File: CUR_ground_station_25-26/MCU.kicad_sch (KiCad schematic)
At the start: 14 parts, among them J4 Conn_01x04_Pin, SW7 PTS815SJM250SMTRLFS, SW8 PTS815SJM250SMTRLFS, U1 ESP32-S3-WROOM-1

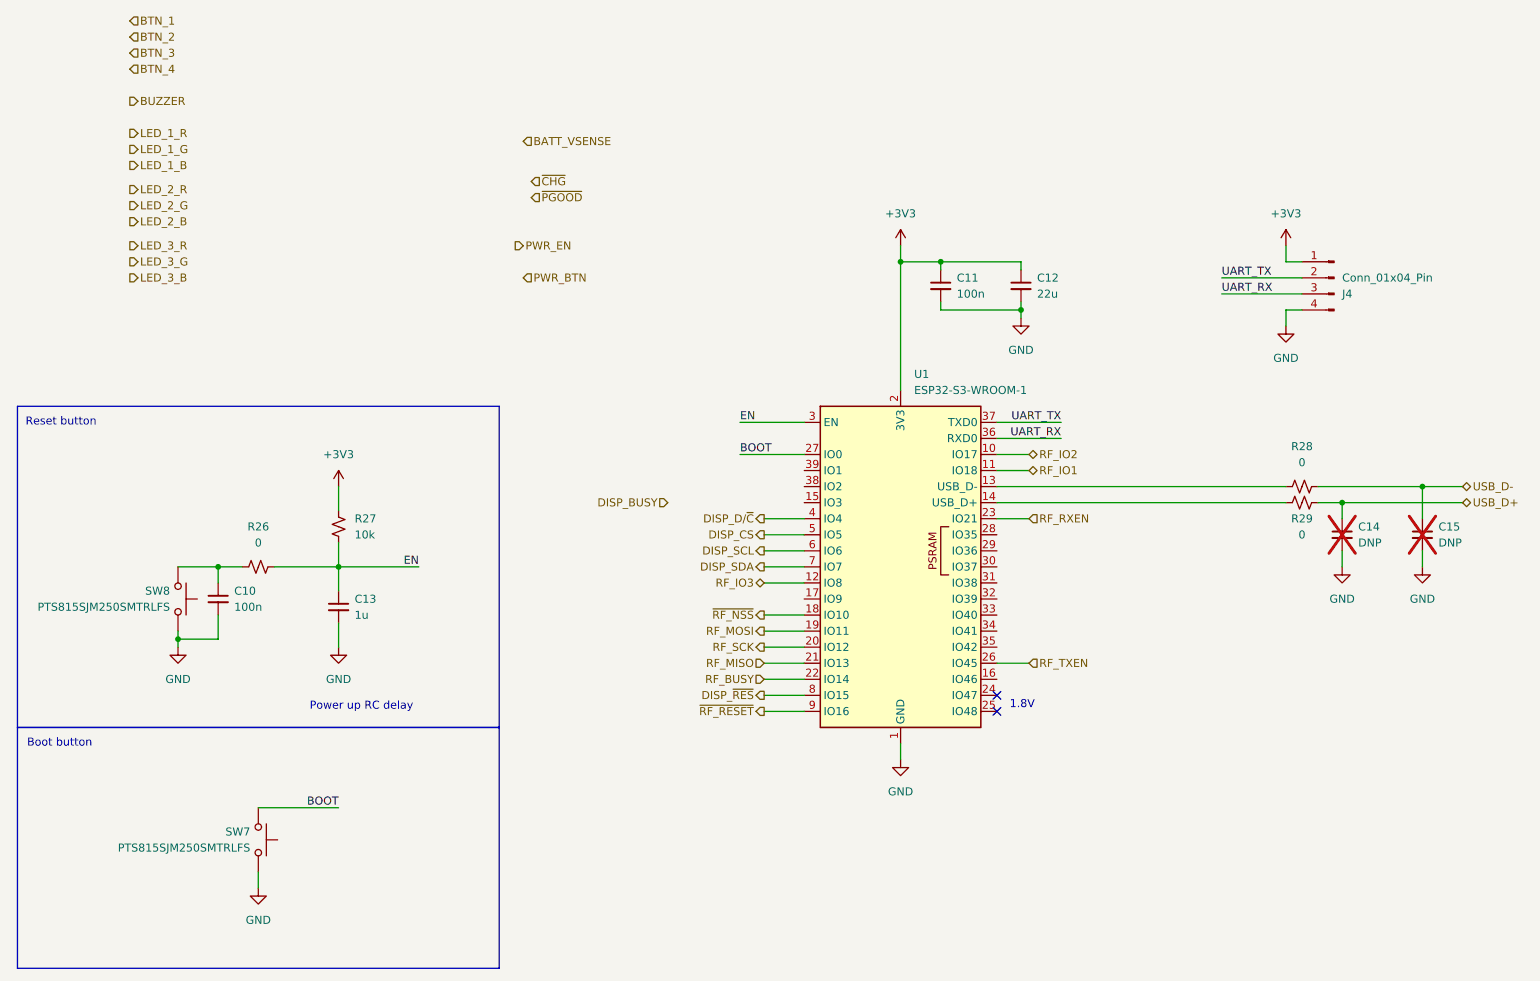
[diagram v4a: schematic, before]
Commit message: Change MCU, hookup more pins
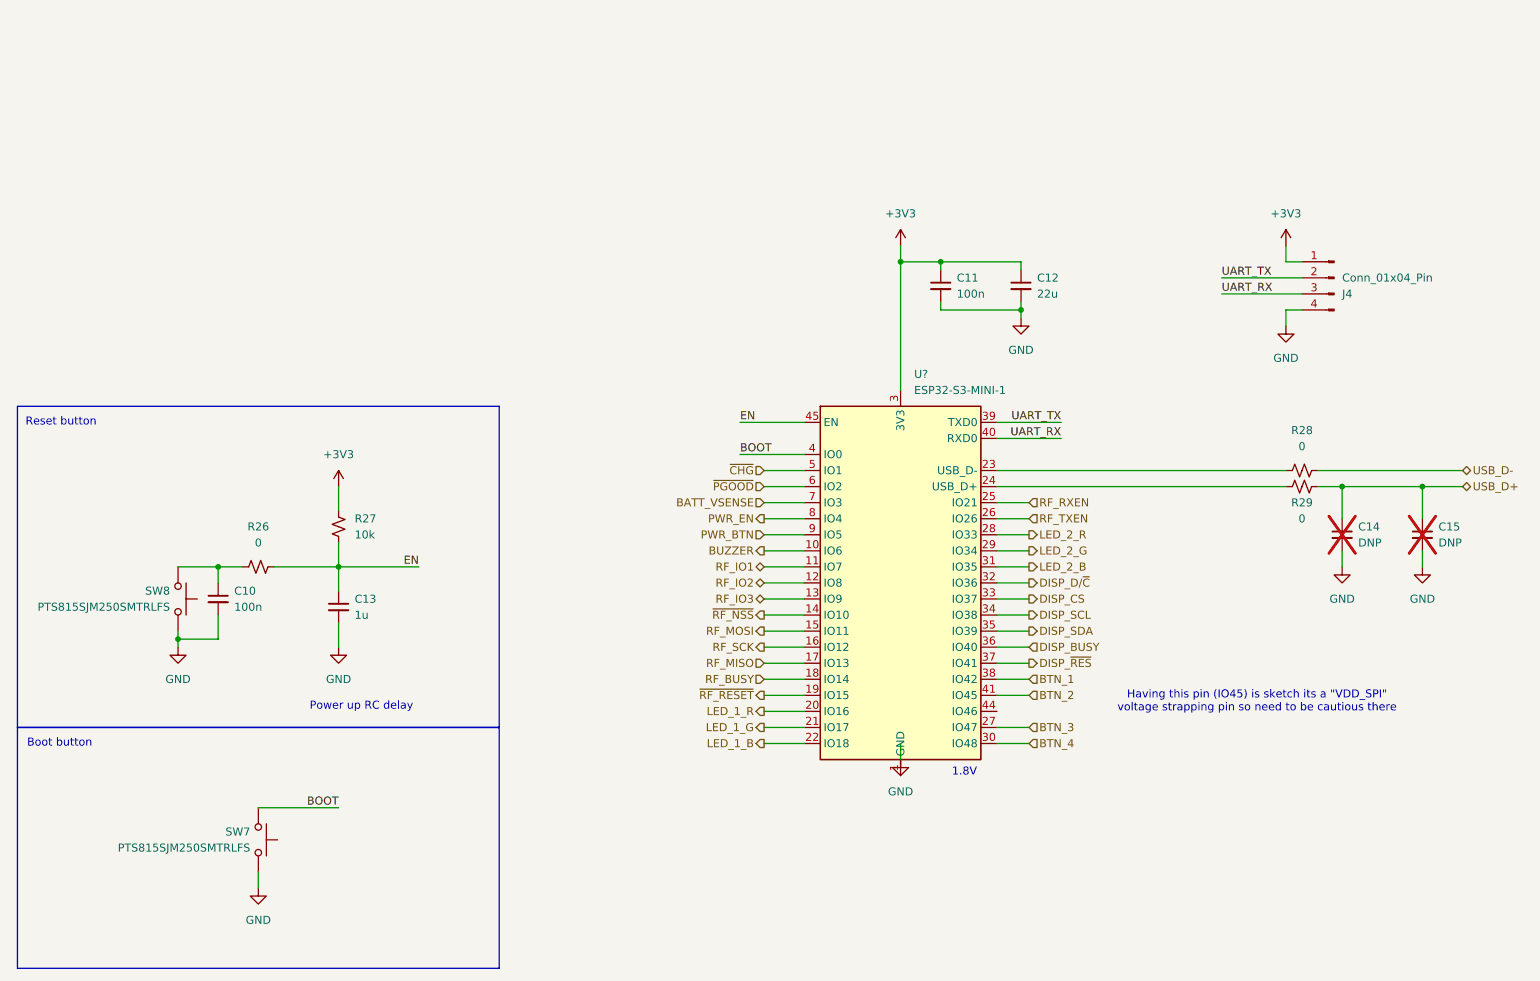
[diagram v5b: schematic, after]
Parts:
- removed U1: ESP32-S3-WROOM-1, RF_Module:ESP32-S3-WROOM-1, symbol RF_Module:ESP32-S3-WROOM-1
- added U?: ESP32-S3-MINI-1, RF_Module:ESP32-S2-MINI-1, symbol RF_Module:ESP32-S3-MINI-1
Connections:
- net +3V3: now also U?.3 (3V3)
- net BATT_VSENSE: now also U?.7 (IO3)
- net BOOT: now also U?.4 (IO0)
- net BTN_1: now also U?.38 (IO42)
- net BTN_2: now also U?.41 (IO45)
- net BTN_3: now also U?.27 (IO47)
- net BTN_4: now also U?.30 (IO48)
- net BUZZER: now also U?.10 (IO6)
- net DISP_BUSY: now also U?.36 (IO40)
- net DISP_CS: now also U?.33 (IO37)
- net DISP_D/~{C}: now also U?.32 (IO36)
- net DISP_SCL: now also U?.34 (IO38)
- net DISP_SDA: now also U?.35 (IO39)
- net DISP_~{RES}: now also U?.37 (IO41)
- net EN: now also U?.45 (EN)
- net LED_1_B: now also U?.22 (IO18)
- net LED_1_G: now also U?.21 (IO17)
- net LED_1_R: now also U?.20 (IO16)
- net LED_2_B: now also U?.31 (IO35)
- net LED_2_G: now also U?.29 (IO34)
- net LED_2_R: now also U?.28 (IO33)
- net PWR_BTN: now also U?.9 (IO5)
- net PWR_EN: now also U?.8 (IO4)
- net RF_BUSY: now also U?.18 (IO14)
- net RF_IO1: now also U?.11 (IO7)
- net RF_IO2: now also U?.12 (IO8)
- net RF_IO3: now also U?.13 (IO9)
- net RF_MISO: now also U?.17 (IO13)
- net RF_MOSI: now also U?.15 (IO11)
- net RF_RXEN: now also U?.25 (IO21)
- net RF_SCK: now also U?.16 (IO12)
- net RF_TXEN: now also U?.26 (IO26)
- net UART_RX: now also U?.40 (RXD0)
- net UART_TX: now also U?.39 (TXD0)
- net USB_D+: now also C15.1
- net USB_D-: no longer C15.1
- net ~{CHG}: now also U?.5 (IO1)
- net ~{PGOOD}: now also U?.6 (IO2)
- net ~{RF_NSS}: now also U?.14 (IO10)
- net ~{RF_RESET}: now also U?.19 (IO15)
- net at R29.1: now also U?.24 (USB_D+)
- net at R28.1: now also U?.23 (USB_D-)
- new net: U?.1 (GND), U?.2 (GND), U?.42 (GND), U?.43 (GND), U?.46 (GND), U?.47 (GND), U?.48 (GND), U?.49 (GND), U?.50 (GND), U?.51 (GND), U?.52 (GND), U?.53 (GND), U?.54 (GND), U?.55 (GND), U?.56 (GND), U?.57 (GND), U?.58 (GND), U?.59 (GND), U?.60 (GND), U?.61 (GND), U?.62 (GND), U?.63 (GND), U?.64 (GND), U?.65 (GND)
- no-connect marks 2 -> 0
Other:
- note added: "Having this pin (IO45) is sketch its a "VDD_SPI" voltage strapping pin so need to be cautious there"
- moved on the sheet: R28, R29

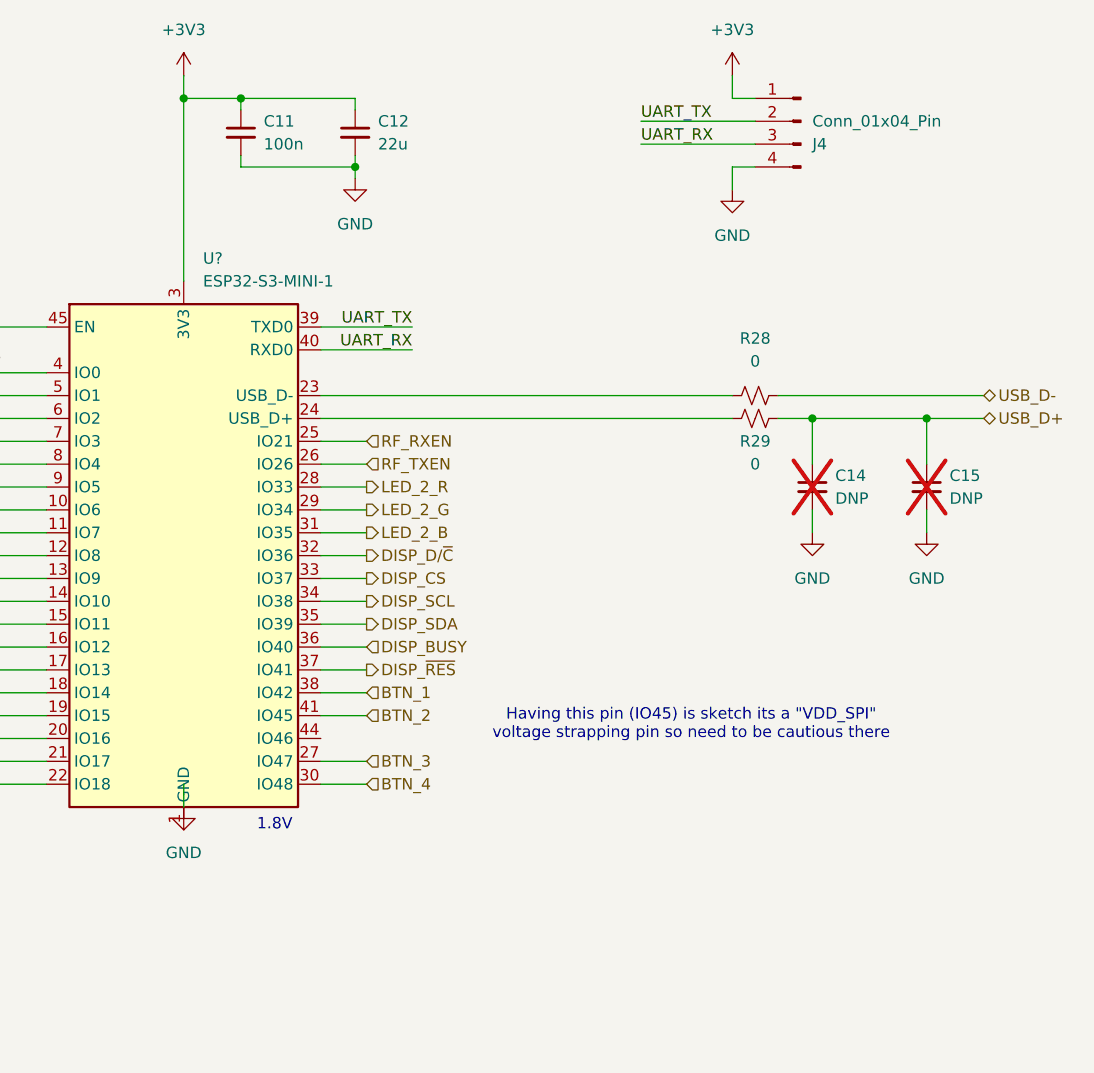
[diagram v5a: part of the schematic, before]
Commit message: updating footprints
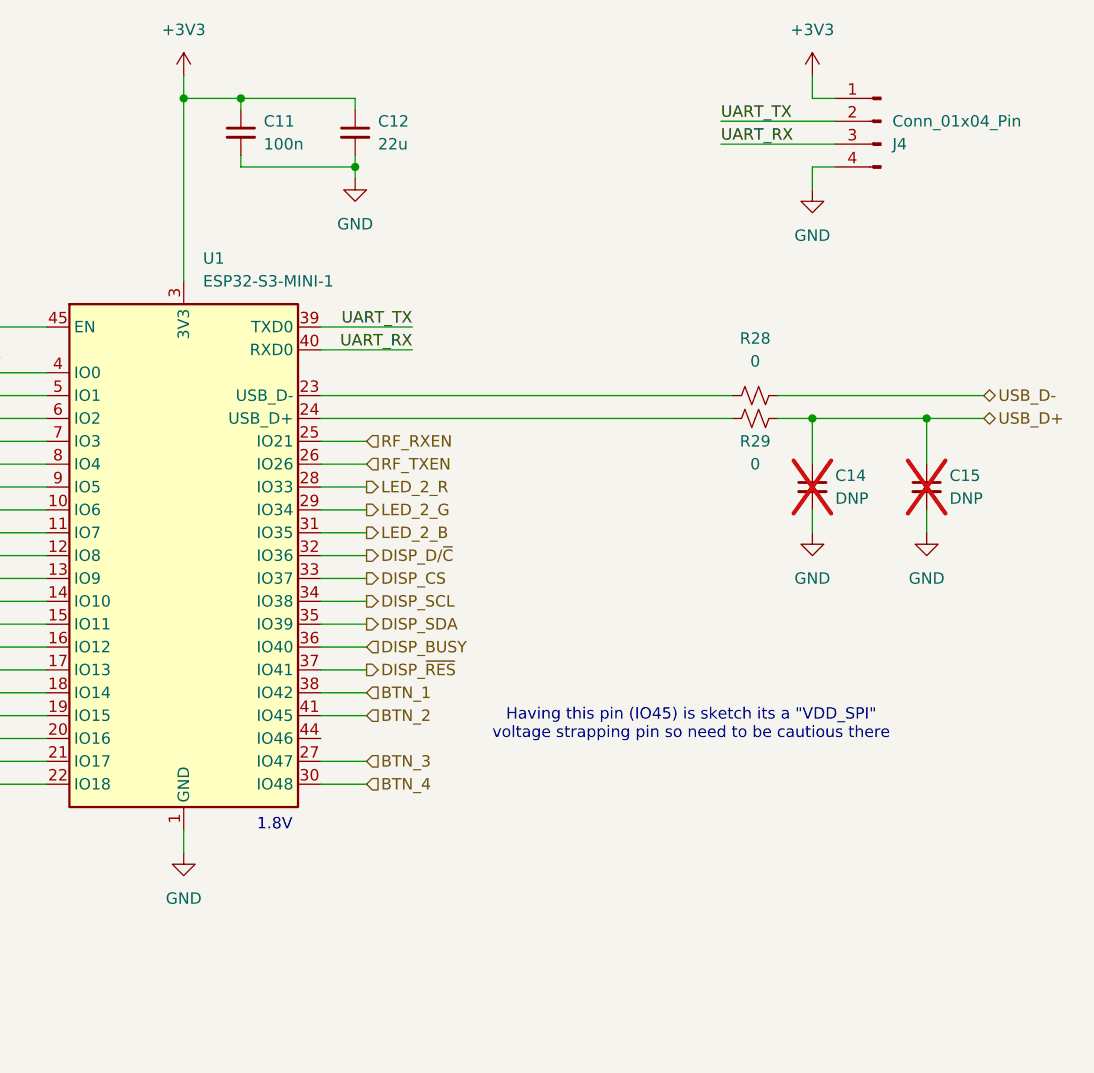
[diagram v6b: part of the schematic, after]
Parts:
- C10, C11, C12, C13, C14, C15: footprint (none) -> Capacitor_SMD:C_0603_1608Metric
- R26, R27, R28, R29: footprint (none) -> Resistor_SMD:R_0603_1608Metric
- SW7, SW8: footprint (none) -> PTS815_SJM_250_SMTR_LFS:SW_Push_PTS815_SJM_250_SMTR_LFS
- gave numbers to parts that had none: 1
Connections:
- net GND: now also U1.1 (GND), U1.2 (GND), U1.42 (GND), U1.43 (GND), U1.46 (GND), U1.47 (GND), U1.48 (GND), U1.49 (GND), U1.50 (GND), U1.51 (GND), U1.52 (GND), U1.53 (GND), U1.54 (GND), U1.55 (GND), U1.56 (GND), U1.57 (GND), U1.58 (GND), U1.59 (GND), U1.60 (GND), U1.61 (GND), U1.62 (GND), U1.63 (GND), U1.64 (GND), U1.65 (GND)
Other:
- moved on the sheet: J4
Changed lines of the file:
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@@
 	(wire
 		(pts
-			(xy 213.36 63.5) (xy 213.36 60.96)
+			(xy 222.25 63.5) (xy 222.25 60.96)
 		)
 		(stroke
@@
 	(wire
 		(pts
-			(xy 152.4 129.54) (xy 152.4 132.08)
-		)
-		(stroke
-			(width 0)
-			(type default)
-		)
-	)
-	(wire
-		(pts
 			(xy 130.81 106.68) (xy 137.16 106.68)
 		)
@@
 	(wire
 		(pts
-			(xy 215.9 55.88) (xy 203.2 55.88)
+			(xy 224.79 55.88) (xy 212.09 55.88)
 		)
 		(stroke
@@
 	(wire
 		(pts
-			(xy 215.9 58.42) (xy 203.2 58.42)
+			(xy 224.79 58.42) (xy 212.09 58.42)
 		)
 		(stroke
@@
 	(wire
 		(pts
+			(xy 152.4 134.62) (xy 152.4 137.16)
+		)
+		(stroke
+			(width 0)
+			(type default)
+		)
+	)
+	(wire
+		(pts
 			(xy 152.4 53.34) (xy 152.4 73.66)
 		)
@@
 	(wire
 		(pts
-			(xy 213.36 60.96) (xy 215.9 60.96)
+			(xy 222.25 60.96) (xy 224.79 60.96)
 		)
 		(stroke
@@
 	(wire
 		(pts
-			(xy 213.36 50.8) (xy 213.36 53.34)
+			(xy 222.25 50.8) (xy 222.25 53.34)
 		)
 		(stroke
@@
 	(wire
 		(pts
-			(xy 213.36 53.34) (xy 215.9 53.34)
+			(xy 222.25 53.34) (xy 224.79 53.34)
 		)
 		(stroke
@@
 	)
 	(label "UART_RX"
-		(at 203.2 58.42 0)
+		(at 212.09 58.42 0)
 		(effects
 			(font
@@
 	)
 	(label "UART_TX"
-		(at 203.2 55.88 0)
+		(at 212.09 55.88 0)
 		(effects
 			(font
@@
 	(symbol
 		(lib_id "Connector:Conn_01x04_Pin")
-		(at 220.98 55.88 0)
+		(at 229.87 55.88 0)
 		(mirror y)
 		(unit 1)
@@
 		(dnp no)
 		(property "Reference" "J4"
-			(at 222.25 58.4201 0)
+			(at 231.14 58.4201 0)
 			(effects
 				(font
@@
 		)
 		(property "Value" "Conn_01x04_Pin"
-			(at 222.25 55.8801 0)
+			(at 231.14 55.8801 0)
 			(effects
 				(font
@@
 		)
 		(property "Footprint" ""
-			(at 220.98 55.88 0)
+			(at 229.87 55.88 0)
 			(effects
 				(font
@@
 		)
 		(property "Datasheet" "~"
-			(at 220.98 55.88 0)
+			(at 229.87 55.88 0)
 			(effects
 				(font
@@
 		)
 		(property "Description" "Generic connector, single row, 01x04, script generated"
-			(at 220.98 55.88 0)
+			(at 229.87 55.88 0)
 			(effects
 				(font
@@
 			)
 		)
-		(property "Footprint" ""
+		(property "Footprint" "Capacitor_SMD:C_0603_1608Metric"
 			(at 234.95 96.52 0)
 			(effects
@@
 			)
 		)
-		(property "Footprint" ""
+		(property "Footprint" "Resistor_SMD:R_0603_1608Metric"
 			(at 215.9 88.9 0)
 			(effects
@@
 	(symbol
 		(lib_id "power:GND")
-		(at 213.36 63.5 0)
+		(at 222.25 63.5 0)
 		(unit 1)
 		(exclude_from_sim no)
@@
 		(fields_autoplaced yes)
 		(property "Reference" "#PWR058"
-			(at 213.36 69.85 0)
+			(at 222.25 69.85 0)
 			(effects
 				(font
@@
 		)
 		(property "Value" "GND"
-			(at 213.36 68.58 0)
+			(at 222.25 68.58 0)
 			(effects
 				(font
@@
 		)
 		(property "Footprint" ""
-			(at 213.36 63.5 0)
+			(at 222.25 63.5 0)
 			(effects
 				(font
@@
 		)
 		(property "Datasheet" ""
-			(at 213.36 63.5 0)
+			(at 222.25 63.5 0)
 			(effects
 				(font
@@
 		)
 		(property "Description" "Power symbol creates a global label with name \"GND\" , ground"
-			(at 213.36 63.5 0)
+			(at 222.25 63.5 0)
 			(effects
 				(font
@@
 			)
 		)
-		(property "Footprint" ""
+		(property "Footprint" "Resistor_SMD:R_0603_1608Metric"
 			(at 215.9 86.36 0)
 			(effects
@@
 			)
 		)
-		(property "Footprint" ""
+		(property "Footprint" "Capacitor_SMD:C_0603_1608Metric"
 			(at 222.25 96.52 0)
 			(effects
@@
 	(symbol
 		(lib_id "power:+3V3")
-		(at 213.36 50.8 0)
+		(at 222.25 50.8 0)
 		(unit 1)
 		(exclude_from_sim no)
@@
 		(fields_autoplaced yes)
 		(property "Reference" "#PWR01"
-			(at 213.36 54.61 0)
+			(at 222.25 54.61 0)
 			(effects
 				(font
@@
 		)
 		(property "Value" "+3V3"
-			(at 213.36 45.72 0)
+			(at 222.25 45.72 0)
 			(effects
 				(font
@@
 		)
 		(property "Footprint" ""
-			(at 213.36 50.8 0)
+			(at 222.25 50.8 0)
 			(effects
 				(font
@@
 		)
 		(property "Datasheet" ""
-			(at 213.36 50.8 0)
+			(at 222.25 50.8 0)
 			(effects
 				(font
@@
 		)
 		(property "Description" "Power symbol creates a global label with name \"+3V3\""
-			(at 213.36 50.8 0)
+			(at 222.25 50.8 0)
 			(effects
 				(font
@@
 			)
 		)
-		(property "Footprint" ""
+		(property "Footprint" "Capacitor_SMD:C_0603_1608Metric"
 			(at 44.45 106.68 0)
 			(effects
@@
 			)
 		)
-		(property "Footprint" ""
+		(property "Footprint" "Capacitor_SMD:C_0603_1608Metric"
 			(at 171.45 57.15 0)
 			(effects
@@
 			)
 		)
-		(property "Footprint" ""
+		(property "Footprint" "Capacitor_SMD:C_0603_1608Metric"
 			(at 63.5 107.95 0)
 			(effects
@@
 			)
 		)
-		(property "Footprint" ""
+		(property "Footprint" "Capacitor_SMD:C_0603_1608Metric"
 			(at 158.75 57.15 0)
 			(effects
@@
 			)
 		)
-		(property "Footprint" ""
+		(property "Footprint" "PTS815_SJM_250_SMTR_LFS:SW_Push_PTS815_SJM_250_SMTR_LFS"
 			(at 55.88 144.78 0)
 			(effects
@@
 	(symbol
 		(lib_id "power:GND")
-		(at 152.4 132.08 0)
+		(at 152.4 137.16 0)
 		(unit 1)
 		(exclude_from_sim no)
@@
 		(fields_autoplaced yes)
 		(property "Reference" "#PWR041"
-			(at 152.4 138.43 0)
+			(at 152.4 143.51 0)
 			(effects
 				(font
@@
 		)
 		(property "Value" "GND"
+			(at 152.4 142.24 0)
+			(effects
+				(font
+					(size 1.27 1.27)
+				)
+			)
+		)
+		(property "Footprint" ""
 			(at 152.4 137.16 0)
 			(effects
@@
 					(size 1.27 1.27)
 				)
-			)
-		)
-		(property "Footprint" ""
-			(at 152.4 132.08 0)
-			(effects
-				(font
-					(size 1.27 1.27)
-				)
 				(hide yes)
 			)
 		)
 		(property "Datasheet" ""
-			(at 152.4 132.08 0)
+			(at 152.4 137.16 0)
 			(effects
 				(font
@@
 		)
 		(property "Description" "Power symbol creates a global label with name \"GND\" , ground"
-			(at 152.4 132.08 0)
+			(at 152.4 137.16 0)
 			(effects
 				(font
@@
 			)
 		)
-		(property "Footprint" ""
+		(property "Footprint" "Resistor_SMD:R_0603_1608Metric"
 			(at 50.8 101.6 0)
 			(effects
@@
 			)
 		)
-		(property "Footprint" ""
+		(property "Footprint" "PTS815_SJM_250_SMTR_LFS:SW_Push_PTS815_SJM_250_SMTR_LFS"
 			(at 43.18 106.68 0)
 			(effects
@@
 		(dnp no)
 		(fields_autoplaced yes)
-		(property "Reference" "U?"
+		(property "Reference" "U1"
 			(at 154.5433 71.12 0)
 			(effects
@@
 			(project ""
 				(path "/b6f682bd-f29b-4650-adb4-b230be0368ad/93f1773d-50f2-4b84-8490-36583ba7e964"
-					(reference "U?")
+					(reference "U1")
 					(unit 1)
 				)
@@
 			)
 		)
-		(property "Footprint" ""
+		(property "Footprint" "Resistor_SMD:R_0603_1608Metric"
 			(at 63.5 95.25 0)
 			(effects

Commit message: added more footprints
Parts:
- J4: footprint (none) -> Connector_PinHeader_2.54mm:PinHeader_1x04_P2.54mm_Vertical
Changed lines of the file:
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@@
 			)
 		)
-		(property "Footprint" ""
+		(property "Footprint" "Connector_PinHeader_2.54mm:PinHeader_1x04_P2.54mm_Vertical"
 			(at 229.87 55.88 0)
 			(effects
